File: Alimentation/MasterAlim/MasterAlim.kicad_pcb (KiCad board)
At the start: 4 copper layers, 76.5 x 90 mm, 99 parts, among them J1 Ext-Con, J10 Interf-Reg1, J11 AU Logic, J12 Interf-Reg2, J13 Interf-Reg3, J14 Interf-Reg4, J2 5V, J3 Bat. IN, J5 Direct Out, J6 Reg 1, J7 Reg 2, J8 Reg 3, J9 Reg 4, U1 74LS33, U2 PCF8591, U3 ACS712xLCTR-20A, U4 PCF8591, U5 PCF8591, U6 PTN78020W_EUK-7, U7 ACS712xLCTR-20A, U8 PCF8574A

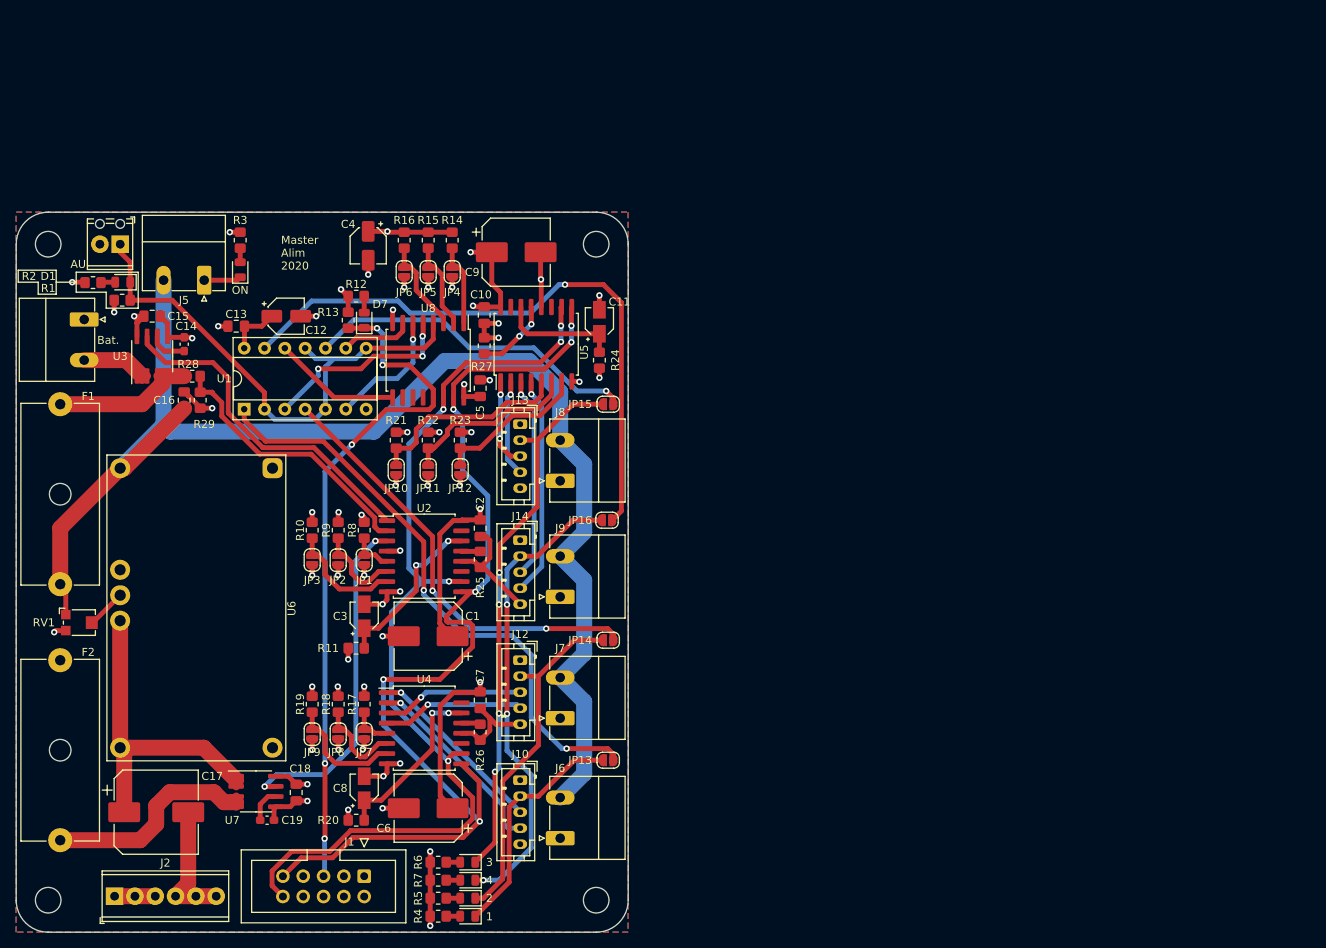
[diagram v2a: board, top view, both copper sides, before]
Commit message: Module alim ISO, clean master alim
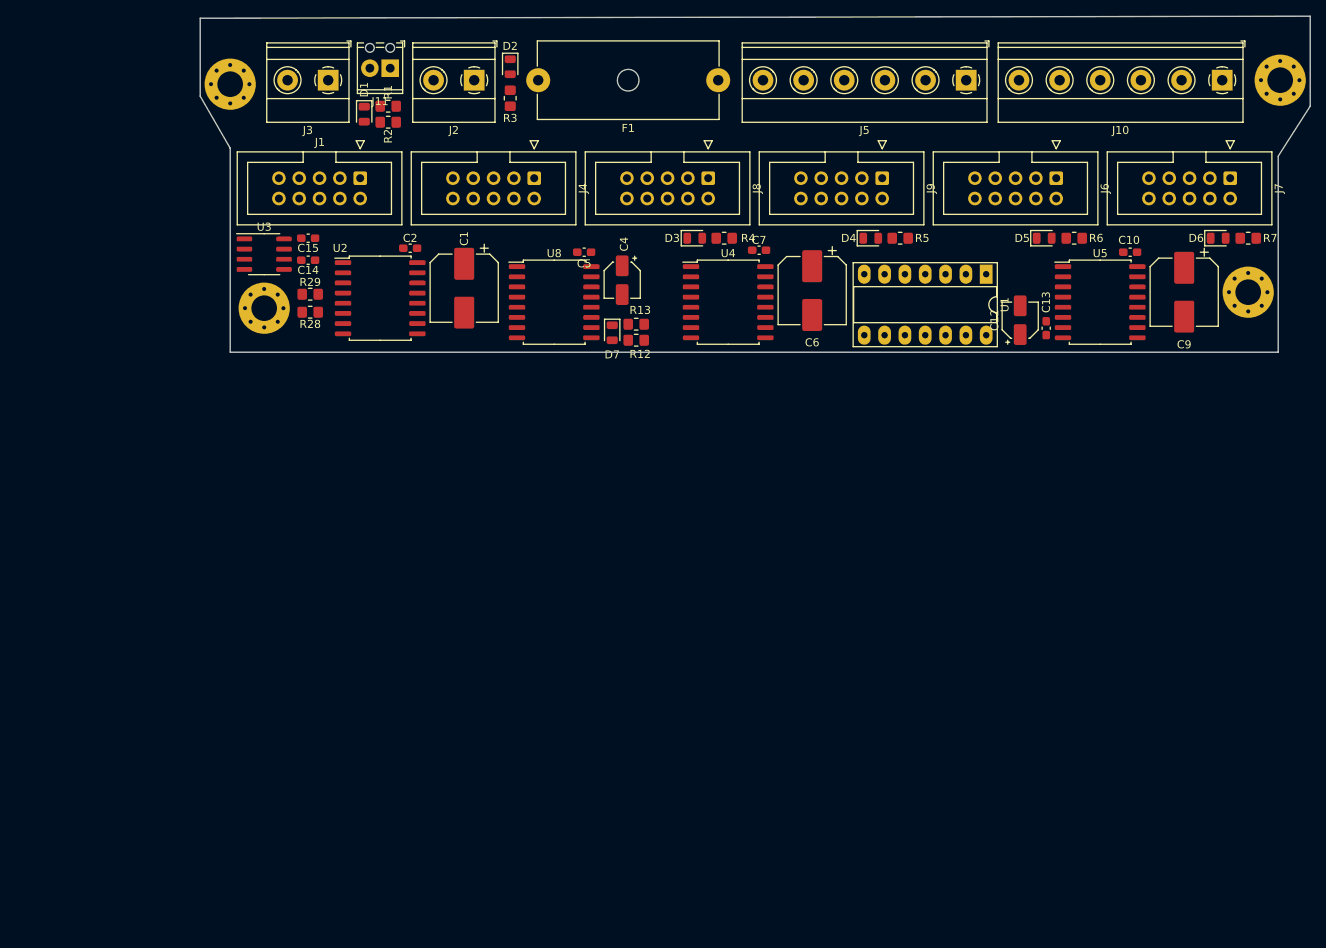
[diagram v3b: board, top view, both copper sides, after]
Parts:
- removed C11, C3, C8: 100u, Capacitor_SMD:CP_Elec_3x5.3
- removed C16: 2.2u, Capacitor_SMD:C_0805_2012Metric_Pad1.18x1.45mm_HandSolder
- removed C17: 330u, Capacitor_SMD:CP_Elec_10x10
- removed C18: 100n, Capacitor_SMD:C_0805_2012Metric_Pad1.18x1.45mm_HandSolder
- removed C19: 1n, Capacitor_SMD:C_0603_1608Metric_Pad1.08x0.95mm_HandSolder
- removed F2: 6A, Fuse:Fuseholder_Cylinder-5x20mm_Schurter_0031_8201_Horizontal_Open
- removed J12: Interf-Reg2, Connector_JST:JST_PH_B5B-PH-K_1x05_P2.00mm_Vertical
- removed J13: Interf-Reg3, Connector_JST:JST_PH_B5B-PH-K_1x05_P2.00mm_Vertical
- removed J14: Interf-Reg4, Connector_JST:JST_PH_B5B-PH-K_1x05_P2.00mm_Vertical
- removed JP1, JP10, JP4, JP7: A0, Jumper:SolderJumper-2_P1.3mm_Open_RoundedPad1.0x1.5mm
- removed JP11, JP2, JP5, JP8: A1, Jumper:SolderJumper-2_P1.3mm_Open_RoundedPad1.0x1.5mm
- removed JP12, JP3, JP6, JP9: A2, Jumper:SolderJumper-2_P1.3mm_Open_RoundedPad1.0x1.5mm
- removed JP13: EN_T1, Jumper:SolderJumper-2_P1.3mm_Open_RoundedPad1.0x1.5mm
- removed JP14: EN_T2, Jumper:SolderJumper-2_P1.3mm_Open_RoundedPad1.0x1.5mm
- removed JP15: EN_T3, Jumper:SolderJumper-2_P1.3mm_Open_RoundedPad1.0x1.5mm
- removed JP16: EN_T4, Jumper:SolderJumper-2_P1.3mm_Open_RoundedPad1.0x1.5mm
- removed R10, R11, R14, R15, R16, R17, R18, R19, R20, R21, R22, R23, R24, R25, R26, R27, R8, R9: 10k, Resistor_SMD:R_0805_2012Metric_Pad1.20x1.40mm_HandSolder
- removed RV1: R_POT_US, Potentiometer_SMD:Potentiometer_Bourns_TC33X_Vertical
- removed U6: PTN78020W_EUK-7, ARIG:Texas_EUK_R-PDSS-T7_THT
- removed U7: ACS712xLCTR-20A, Package_SO:SOIC-8_3.9x4.9mm_P1.27mm
- added J4: Reg 1, Connector_IDC:IDC-Header_2x05_P2.54mm_Vertical, F.Cu at (163.2, 45.2)
- C10, C13, C15, C2, C5, C7: footprint Capacitor_SMD:C_0805_2012Metric_Pad1.18x1.45mm_HandSolder -> Capacitor_SMD:C_0603_1608Metric_Pad1.08x0.95mm_HandSolder
- H1, H2, H3, H4: value MountingHole -> MountingHole_Pad; footprint MountingHole:MountingHole_3.2mm_M3 -> MountingHole:MountingHole_3.2mm_M3_Pad_Via
- J10: value Interf-Reg1 -> Batt GND; footprint Connector_JST:JST_PH_B5B-PH-K_1x05_P2.00mm_Vertical -> TerminalBlock_Phoenix:TerminalBlock_Phoenix_MKDS-1,5-6-5.08_1x06_P5.08mm_Horizontal
- J2: value 5V -> Alim logique; footprint TerminalBlock_Phoenix:TerminalBlock_Phoenix_MPT-0,5-6-2.54_1x06_P2.54mm_Horizontal -> TerminalBlock_Phoenix:TerminalBlock_Phoenix_MKDS-1,5-2-5.08_1x02_P5.08mm_Horizontal
- J3: value Bat. IN -> Batt IN; footprint Connector_Phoenix_MC_HighVoltage:PhoenixContact_MC_1,5_2-G-5.08_1x02_P5.08mm_Horizontal -> TerminalBlock_Phoenix:TerminalBlock_Phoenix_MKDS-1,5-2-5.08_1x02_P5.08mm_Horizontal
- J5: value Direct Out -> Batt +; footprint Connector_Phoenix_MC_HighVoltage:PhoenixContact_MC_1,5_2-G-5.08_1x02_P5.08mm_Horizontal -> TerminalBlock_Phoenix:TerminalBlock_Phoenix_MKDS-1,5-6-5.08_1x06_P5.08mm_Horizontal
- J6: value Reg 1 -> Reg 3; footprint Connector_Phoenix_MC_HighVoltage:PhoenixContact_MC_1,5_2-G-5.08_1x02_P5.08mm_Horizontal -> Connector_IDC:IDC-Header_2x05_P2.54mm_Vertical
- J7: value Reg 2 -> Reg 4; footprint Connector_Phoenix_MC_HighVoltage:PhoenixContact_MC_1,5_2-G-5.08_1x02_P5.08mm_Horizontal -> Connector_IDC:IDC-Header_2x05_P2.54mm_Vertical
- J8: value Reg 3 -> Reg 1; footprint Connector_Phoenix_MC_HighVoltage:PhoenixContact_MC_1,5_2-G-5.08_1x02_P5.08mm_Horizontal -> Connector_IDC:IDC-Header_2x05_P2.54mm_Vertical
- J9: value Reg 4 -> Reg 2; footprint Connector_Phoenix_MC_HighVoltage:PhoenixContact_MC_1,5_2-G-5.08_1x02_P5.08mm_Horizontal -> Connector_IDC:IDC-Header_2x05_P2.54mm_Vertical
- U1: footprint Package_DIP:DIP-14_W7.62mm_Socket -> Package_DIP:DIP-14_W7.62mm_Socket_LongPads
- moved R7 129.2 mm to (252.5, 52.8), turned to 180 degrees
- moved J10 123.9 mm to (249.2, 33.0), turned to 180 degrees
- moved D6 123.4 mm to (248.8, 52.8), turned to 0 degrees
- moved J2 111.5 mm to (155.8, 33.0), turned to 180 degrees
- moved H4 111.4 mm to (252.5, 59.5)
- moved R6 111.4 mm to (230.8, 52.8), turned to 180 degrees
- moved J7 107.6 mm to (250.2, 45.2), turned to 270 degrees
- moved D5 106.2 mm to (227.0, 52.8), turned to 0 degrees
- moved F1 103.6 mm to (186.2, 33.0), turned to 180 degrees
- moved J6 103.2 mm to (228.5, 45.2), turned to 270 degrees
- moved C13 101.3 mm to (227.2, 64.0), turned to 90 degrees
- moved R5 100.7 mm to (209.0, 52.8), turned to 180 degrees
- moved J5 98.5 mm to (217.2, 33.0)
- moved D4 96.7 mm to (205.3, 52.8), turned to 0 degrees
- moved U1 94.3 mm to (219.8, 57.2), turned to 270 degrees
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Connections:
- H1 pad 1: (no net) -> GND
- H2 pad 1: (no net) -> GND
- H3 pad 1: (no net) -> GND
- H4 pad 1: (no net) -> GND
- J10 pad 1: +5V -> GND
- J10 pad 2: /EN_T1 -> GND
- J10 pad 3: /ANA_T1_CURRENT -> GND
- J10 pad 4: /ANA_T1_VOLT -> GND
- J2 pad 2: +5V -> GND
- J3 pad 1: GND -> /BatIN
- J3 pad 2: Net-(J3-Pad2) -> GND
- J5 pad 1: GND -> +BATT
- J6 pad 1: GND -> +5V
- J6 pad 2: +BATT -> +5V
- J7 pad 1: GND -> +5V
- J7 pad 2: +BATT -> +5V
- J8 pad 1: GND -> +5V
- J8 pad 2: +BATT -> +5V
- J9 pad 1: GND -> +5V
- J9 pad 2: +BATT -> +5V
- U1 pad 1: Net-(JP13-Pad1) -> /EN_T1
- U1 pad 10: Net-(JP15-Pad1) -> /EN_T3
- U1 pad 13: Net-(JP16-Pad1) -> /EN_T4
- U1 pad 4: Net-(JP14-Pad1) -> /EN_T2
- U2 pad 13: Net-(R25-Pad1) -> GND
- U2 pad 14: Net-(C3-Pad1) -> +5V
- U2 pad 3: /ANA_5V_CURRENT -> /ANA_LOG_CURRENT
- U2 pad 4: +5V -> /ANA_LOG_VOLT
- U2 pad 5: /AnalogConverter1/A0 -> GND
- U2 pad 6: /AnalogConverter1/A1 -> GND
- U2 pad 7: /AnalogConverter1/A2 -> GND
- U3 pad 1: Net-(J3-Pad2) -> /BatIN
- U3 pad 2: Net-(J3-Pad2) -> /BatIN
- U4 pad 13: Net-(R26-Pad1) -> GND
- U4 pad 14: Net-(C8-Pad1) -> +5V
- U4 pad 5: /AnalogConverter2/A0 -> +5V
- U4 pad 6: /AnalogConverter2/A1 -> GND
- U4 pad 7: /AnalogConverter2/A2 -> GND
- U5 pad 13: Net-(R27-Pad1) -> GND
- U5 pad 14: Net-(C11-Pad1) -> +5V
- U5 pad 5: /AnalogConverter3/A0 -> GND
- U5 pad 6: /AnalogConverter3/A1 -> +5V
- U5 pad 7: /AnalogConverter3/A2 -> GND
- U8 pad 1: /IOExpander1/A0 -> GND
- U8 pad 2: /IOExpander1/A1 -> GND
- U8 pad 3: /IOExpander1/A2 -> GND
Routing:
- net +BATT: track 171.9 -> 0.00 mm
- net SDA: track 134.1 -> 0.00 mm, vias 6 -> 0
- net +5V: track 124.0 -> 0.00 mm, vias 27 -> 0
- net SCL: track 122.4 -> 0.00 mm, vias 5 -> 0
- net GND: track 120.8 -> 0.00 mm, vias 32 -> 0
- net /IRQ: track 85.8 -> 0.00 mm, vias 5 -> 0
- net Net-(JP16-Pad1): track 77.8 -> 0.00 mm, vias 1 -> 0
- net Net-(JP13-Pad1): track 74.0 -> 0.00 mm, vias 2 -> 0
- net /EN_T3: track 68.2 -> 0.00 mm, vias 4 -> 0
- net /AU: track 66.2 -> 0.00 mm
- net /EN_T4: track 59.1 -> 0.00 mm, vias 3 -> 0
- net Net-(JP14-Pad1): track 54.9 -> 0.00 mm, vias 2 -> 0
- net /EN_T2: track 43.8 -> 0.00 mm
- net /ANA_5V_CURRENT: track 42.8 -> 0.00 mm, vias 2 -> 0
- net /ANA_BAT_CURRENT: track 42.7 -> 0.00 mm
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- removed copper zone on In2.Cu, net +5V
- removed copper zone on B.Cu, net GND
- removed copper zone on F.Cu, net GND
- removed copper zone on In1.Cu, net GND
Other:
- board size 76.5 x 90 mm -> 138.8 x 42 mm
- board text removed: "Master Alim 2020"

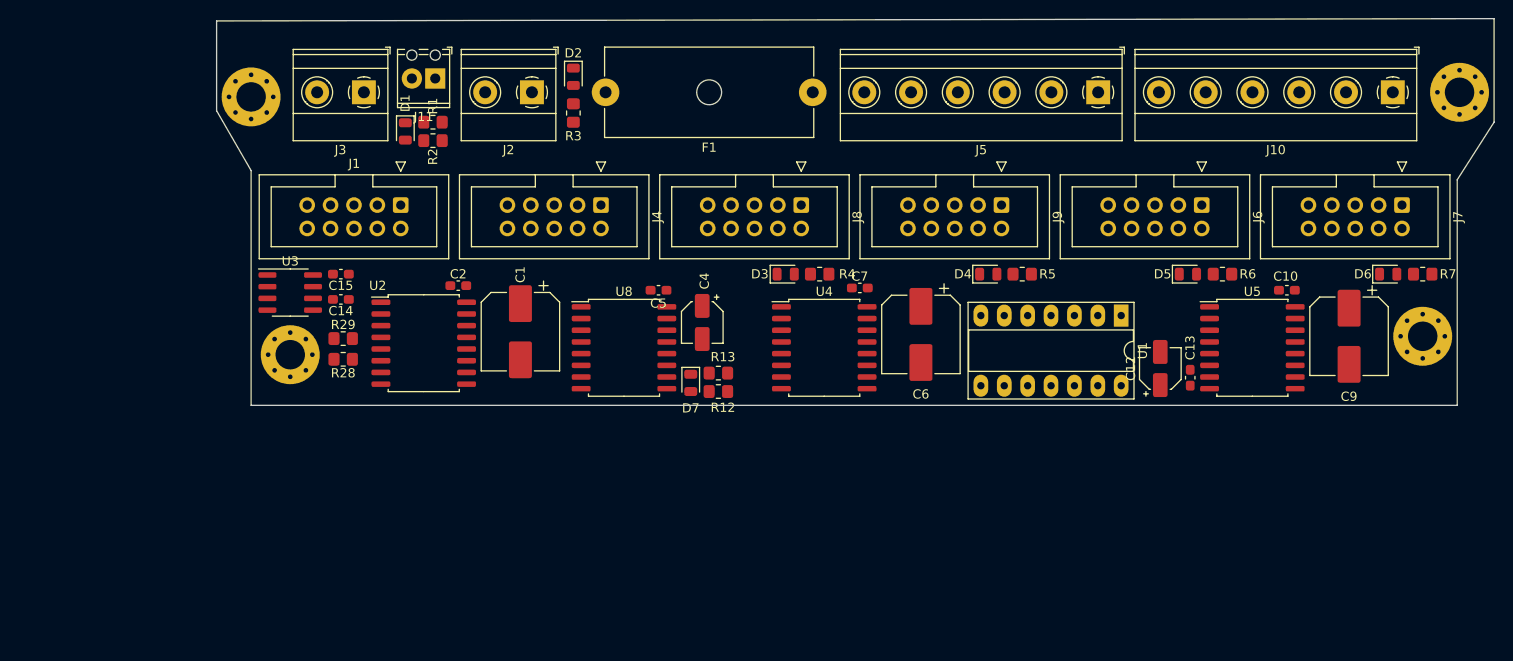
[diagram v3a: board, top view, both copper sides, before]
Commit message: Finalisation modules 3A et 6A, routage master alim
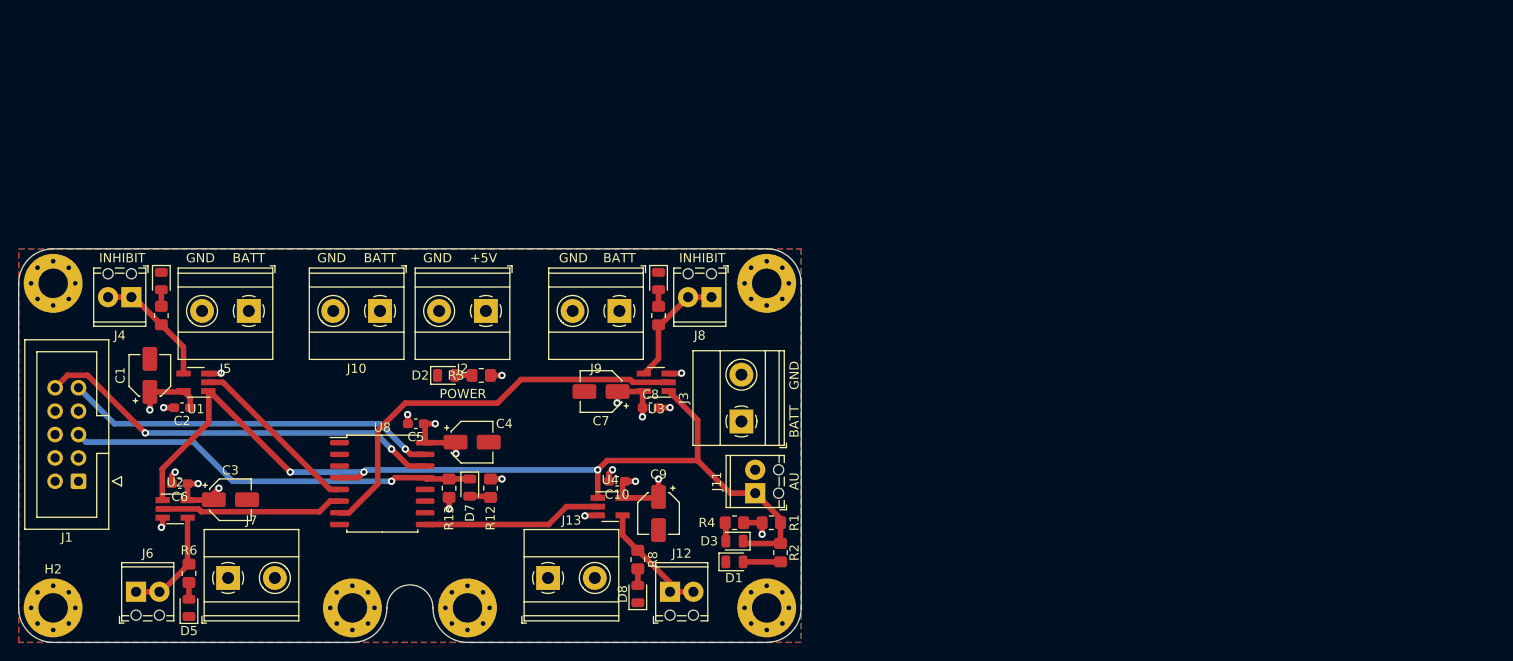
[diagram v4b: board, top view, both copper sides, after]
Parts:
- removed C12: 1u, Capacitor_SMD:CP_Elec_4x5.3
- removed C13, C15: 100n, Capacitor_SMD:C_0603_1608Metric_Pad1.08x0.95mm_HandSolder
- removed C14: 1n, Capacitor_SMD:C_0603_1608Metric_Pad1.08x0.95mm_HandSolder
- removed F1: 10A, Fuse:Fuseholder_Cylinder-5x20mm_Schurter_0031_8201_Horizontal_Open
- removed H3: MountingHole_Pad, MountingHole:MountingHole_3.2mm_M3_Pad_Via
- removed R28: 820k, Resistor_SMD:R_0805_2012Metric_Pad1.20x1.40mm_HandSolder
- removed R29: 130k, Resistor_SMD:R_0805_2012Metric_Pad1.20x1.40mm_HandSolder
- removed U5: PCF8591, Package_SO:SOIC-16W_7.5x10.3mm_P1.27mm
- added C3: 1u, Capacitor_SMD:CP_Elec_4x5.3, F.Cu at (123.0, 77.2)
- added C8: 100n, Capacitor_SMD:C_0603_1608Metric_Pad1.08x0.95mm_HandSolder, F.Cu at (168.6, 67.2)
- added D8: ENABLE REGUL, LED_SMD:LED_0805_2012Metric, F.Cu at (167.2, 87.5)
- added G***: LOGO, ARIG:Logo_ARIG_12_6x6_6, B.Cu at (143.0, 71.2)
- added H6: MountingHole_Pad, MountingHole:MountingHole_3.2mm_M3_Pad_Via, F.Cu at (148.8, 89.0)
- added H7: MountingHole_Pad, MountingHole:MountingHole_3.2mm_M3_Pad_Via, F.Cu at (181.2, 53.8)
- added H8: MountingHole_Pad, MountingHole:MountingHole_3.2mm_M3_Pad_Via, F.Cu at (181.2, 89.0)
- added J12: INHIBIT, TerminalBlock_Phoenix:TerminalBlock_Phoenix_MPT-0,5-2-2.54_1x02_P2.54mm_Horizontal, F.Cu at (170.8, 87.2)
- added J13: ToRegul, TerminalBlock_Phoenix:TerminalBlock_Phoenix_MKDS-1,5-2-5.08_1x02_P5.08mm_Horizontal, F.Cu at (157.5, 85.8)
- added R8: 150, Resistor_SMD:R_0805_2012Metric_Pad1.20x1.40mm_HandSolder, F.Cu at (167.2, 83.8)
- C1, C9: value 100u -> 1u; footprint Capacitor_SMD:CP_Elec_8x6.5 -> Capacitor_SMD:CP_Elec_4x5.3
- C6: value 100u -> 100n; footprint Capacitor_SMD:CP_Elec_8x6.5 -> Capacitor_SMD:C_0603_1608Metric_Pad1.08x0.95mm_HandSolder
- C7: value 100n -> 1u; footprint Capacitor_SMD:C_0603_1608Metric_Pad1.08x0.95mm_HandSolder -> Capacitor_SMD:CP_Elec_4x5.3
- D1: value AU -> AU KO
- D3: value T1 -> AU OK
- D4: value T2 -> ENABLE REGUL
- D5: value T3 -> ENABLE REGUL
- D6: value T4 -> ENABLE REGUL
- J10: value Batt GND -> Reg Log; footprint TerminalBlock_Phoenix:TerminalBlock_Phoenix_MKDS-1,5-6-5.08_1x06_P5.08mm_Horizontal -> TerminalBlock_Phoenix:TerminalBlock_Phoenix_MKDS-1,5-2-5.08_1x02_P5.08mm_Horizontal
- J4, J8: value Reg 1 -> INHIBIT; footprint Connector_IDC:IDC-Header_2x05_P2.54mm_Vertical -> TerminalBlock_Phoenix:TerminalBlock_Phoenix_MPT-0,5-2-2.54_1x02_P2.54mm_Horizontal
- J5: value Batt + -> ToRegul; footprint TerminalBlock_Phoenix:TerminalBlock_Phoenix_MKDS-1,5-6-5.08_1x06_P5.08mm_Horizontal -> TerminalBlock_Phoenix:TerminalBlock_Phoenix_MKDS-1,5-2-5.08_1x02_P5.08mm_Horizontal
- J6: value Reg 3 -> INHIBIT; footprint Connector_IDC:IDC-Header_2x05_P2.54mm_Vertical -> TerminalBlock_Phoenix:TerminalBlock_Phoenix_MPT-0,5-2-2.54_1x02_P2.54mm_Horizontal
- J7: value Reg 4 -> ToRegul; footprint Connector_IDC:IDC-Header_2x05_P2.54mm_Vertical -> TerminalBlock_Phoenix:TerminalBlock_Phoenix_MKDS-1,5-2-5.08_1x02_P5.08mm_Horizontal
- J9: value Reg 2 -> ToRegul; footprint Connector_IDC:IDC-Header_2x05_P2.54mm_Vertical -> TerminalBlock_Phoenix:TerminalBlock_Phoenix_MKDS-1,5-2-5.08_1x02_P5.08mm_Horizontal
- R12, R2: value 220 -> 150
- R3: value 150 -> 220
- R4: value 180 -> 220
- R5, R6, R7: value 180 -> 150
- U1: value 74LS33 -> 74LVC1G02; footprint Package_DIP:DIP-14_W7.62mm_Socket_LongPads -> Package_TO_SOT_SMD:SOT-23-5_HandSoldering
- U2, U4: value PCF8591 -> 74LVC1G02; footprint Package_SO:SOIC-16W_7.5x10.3mm_P1.27mm -> Package_TO_SOT_SMD:SOT-23-5_HandSoldering
- U3: value ACS712xLCTR-20A -> 74LVC1G02; footprint Package_SO:SOIC-8_3.9x4.9mm_P1.27mm -> Package_TO_SOT_SMD:SOT-23-5_HandSoldering
- moved J7 133.8 mm to (122.8, 85.8), turned to 0 degrees
- moved J6 123.1 mm to (112.8, 87.2), turned to 0 degrees
- moved H4 119.9 mm to (136.2, 89.0)
- moved R6 116.9 mm to (118.5, 85.2), turned to 270 degrees
- moved D5 114.4 mm to (118.5, 89.0), turned to 90 degrees
- moved J10 112.5 mm to (139.2, 56.8)
- moved U1 100.8 mm to (119.2, 64.5), turned to 180 degrees
- moved J5 95.3 mm to (125.0, 56.8)
- moved R5 93.6 mm to (115.5, 57.2), turned to 90 degrees
- moved D4 89.8 mm to (115.5, 53.5), turned to 270 degrees
- moved R7 83.1 mm to (169.5, 57.2), turned to 90 degrees
- moved C6 82.1 mm to (117.5, 75.5), turned to 180 degrees
- moved D6 79.3 mm to (169.5, 53.5), turned to 270 degrees
- moved C9 77.4 mm to (169.5, 78.8)
- moved C10 75.7 mm to (165.0, 75.2)
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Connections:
- D1 pad 1: /AU -> GND
- D3 pad 1: /EN_T1 -> /AU
- D4 pad 1: /EN_T2 -> GND
- D5 pad 1: /EN_T3 -> GND
- D6 pad 1: /EN_T4 -> GND
- J10 pad 1: GND -> +BATT
- J3 pad 1: /BatIN -> +BATT
- J4 pad 1: +5V -> /PilAlim1/Y
- J4 pad 2: +5V -> /PilAlim1/Y
- J5 pad 2: +BATT -> GND
- J6 pad 1: +5V -> /sheet602E5506/Y
- J6 pad 2: +5V -> /sheet602E5506/Y
- J7 pad 1: +5V -> +BATT
- J7 pad 2: +5V -> GND
- J8 pad 1: +5V -> /sheet602E5F64/Y
- J8 pad 2: +5V -> /sheet602E5F64/Y
- J9 pad 1: +5V -> +BATT
- J9 pad 2: +5V -> GND
- R2 pad 1: +5V -> /AU
- R5 pad 1: +5V -> /PilAlim1/Y
- R6 pad 1: +5V -> /sheet602E5506/Y
- R7 pad 1: +5V -> /sheet602E5F64/Y
- U1 pad 1: /EN_T1 -> /AU
- U1 pad 2: /AU -> /PIL_T1
- U1 pad 3: /PIL_T1 -> GND
- U1 pad 4: /EN_T2 -> /PilAlim1/Y
- U1 pad 5: /AU -> +5V
- U2 pad 1: /ANA_BAT_CURRENT -> /AU
- U2 pad 2: /ANA_BAT_VOLT -> /PIL_T2
- U2 pad 3: /ANA_LOG_CURRENT -> GND
- U2 pad 4: /ANA_LOG_VOLT -> /sheet602E5506/Y
- U2 pad 5: GND -> +5V
- U3 pad 1: /BatIN -> /AU
- U3 pad 2: /BatIN -> /PIL_T3
- U3 pad 3: /BAT_IN -> GND
- U3 pad 4: /BAT_IN -> /sheet602E5F64/Y
- U3 pad 5: GND -> +5V
- U4 pad 1: /ANA_T1_CURRENT -> /AU
- U4 pad 2: /ANA_T1_VOLT -> /PIL_T4
- U4 pad 3: /ANA_T2_CURRENT -> GND
- U4 pad 4: /ANA_T2_VOLT -> /sheet602E5F6A/Y
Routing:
- net /AU: track 0.00 -> 104.6 mm, vias 0 -> 3
- net +5V: track 0.00 -> 45.9 mm, vias 0 -> 13
- net /PIL_T3: track 0.00 -> 45.3 mm
- net SCL: track 0.00 -> 44.8 mm, vias 0 -> 2
- net /IRQ: track 0.00 -> 44.8 mm, vias 0 -> 1
- net SDA: track 0.00 -> 40.6 mm, vias 0 -> 1
- net /PIL_T2: track 0.00 -> 19.8 mm
- net /PIL_T4: track 0.00 -> 19.6 mm
- net /PIL_T1: track 0.00 -> 19.1 mm
- net /PilAlim1/Y: track 0.00 -> 13.3 mm
- net /sheet602E5F6A/Y: track 0.00 -> 13.0 mm
- net /sheet602E5F64/Y: track 0.00 -> 13.0 mm
- net /sheet602E5506/Y: track 0.00 -> 12.1 mm
- net GND: track 0.00 -> 11.6 mm, vias 0 -> 9
- net Net-(D1-Pad2): track 0.00 -> 4.06 mm
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- added copper zone on In1.Cu, net +5V
- added copper zone on In2.Cu, net +BATT
- added copper zone on B.Cu, net GND
- added copper zone on F.Cu, net GND
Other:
- board size 138.8 x 42 mm -> 85 x 42.8 mm
- board text added: "+5V"
- board text added: "AU"
- board text added: "Alimentation Pilotage regulateur 2020"
- board text added: "BATT"
- board text added: "GND"
- board text added: "INHIBIT"
- board text added: "POWER"
